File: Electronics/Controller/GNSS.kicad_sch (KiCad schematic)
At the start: 10 parts, among them J2 Conn_01x02, J3 Conn_01x02, J4 Conn_01x02, J5 Conn_01x02, J6 GPS SIM, J7 Conn_01x02, J8 Conn_01x02, U1 simpleRTK2B, U2 simpleRTK2B, U4 simpleRTK2B

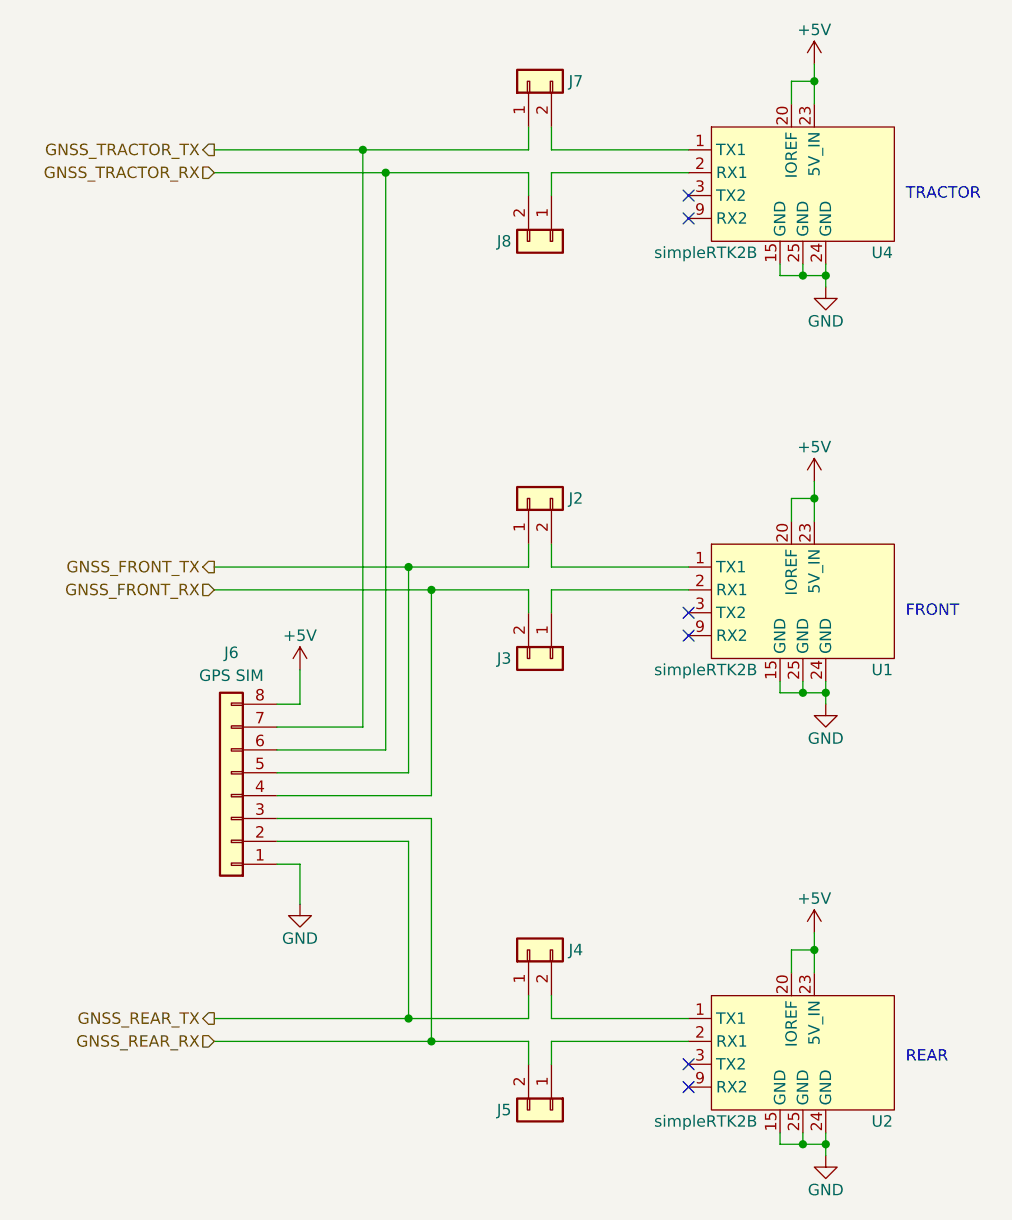
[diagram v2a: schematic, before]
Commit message: Updated schematic. Added footprints for all components.
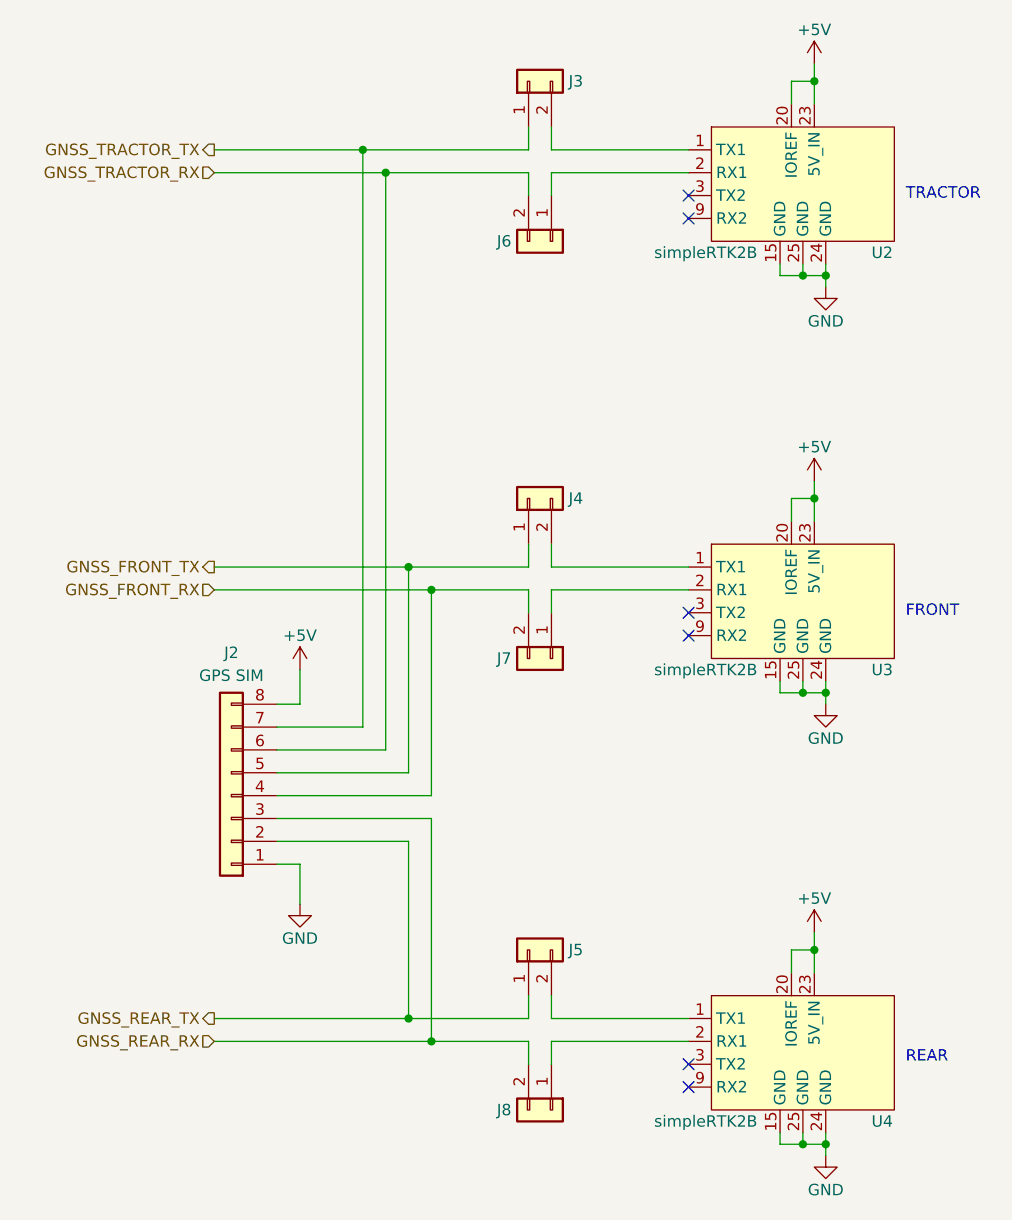
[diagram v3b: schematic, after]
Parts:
- J2: renamed from J6; footprint (none) -> Connector_PinHeader_2.54mm:PinHeader_2x04_P2.54mm_Vertical
- J3: renamed from J7; footprint (none) -> Connector_PinHeader_2.54mm:PinHeader_1x02_P2.54mm_Vertical
- J4: renamed from J2; footprint (none) -> Connector_PinHeader_2.54mm:PinHeader_1x02_P2.54mm_Vertical
- J5: renamed from J4; footprint (none) -> Connector_PinHeader_2.54mm:PinHeader_1x02_P2.54mm_Vertical
- J6: renamed from J8; footprint (none) -> Connector_PinHeader_2.54mm:PinHeader_1x02_P2.54mm_Vertical
- J7: renamed from J3; footprint (none) -> Connector_PinHeader_2.54mm:PinHeader_1x02_P2.54mm_Vertical
- J8: renamed from J5; footprint (none) -> Connector_PinHeader_2.54mm:PinHeader_1x02_P2.54mm_Vertical
- renumbered U4 to U2, U1 to U3, U2 to U4

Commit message: Moved controls from GPIO to CAN bus. Added two more CAN bus connectors. Changed GNSS SIM connector from pin header to JST-PH.
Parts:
- J2: footprint Connector_PinHeader_2.54mm:PinHeader_2x04_P2.54mm_Vertical -> Connector_JST:JST_PH_B8B-PH-K_1x08_P2.00mm_Vertical; manf# (none) -> B8B-PH-K-S
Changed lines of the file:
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@@
   (title_block
     (title "Tandem Leveller Controller")
-    (date "2025-02-19")
+    (date "2025-02-22")
     (rev "V1.0")
     (company "(C) andy@britishideas.com 2025")
@@
       (effects (font (size 1.27 1.27)))
     )
-    (property "Footprint" "Connector_PinHeader_2.54mm:PinHeader_2x04_P2.54mm_Vertical" (at 118.11 110.49 0)
+    (property "Footprint" "Connector_JST:JST_PH_B8B-PH-K_1x08_P2.00mm_Vertical" (at 118.11 110.49 0)
       (effects (font (size 1.27 1.27)) hide)
     )
@@
       (effects (font (size 1.27 1.27)) hide)
     )
+    (property "manf#" "B8B-PH-K-S" (at 118.11 110.49 0)
+      (effects (font (size 1.27 1.27)) hide)
+    )

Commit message: Added 4.7uF caps to FT232RL on controller.
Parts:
- J2: LCSC (none) -> C157974
- J3, J4, J5, J6, J7, J8: LCSC (none) -> C7494857
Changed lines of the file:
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@@
   (title_block
     (title "Tandem Leveller Controller")
-    (date "2025-02-22")
+    (date "2025-03-11")
     (rev "V1.0")
     (company "(C) andy@britishideas.com 2025")
@@
       (effects (font (size 1.27 1.27)) hide)
     )
+    (property "LCSC" "C7494857" (at 153.67 48.895 0)
+      (effects (font (size 1.27 1.27)) hide)
+    )
     (pin "2")
     (pin "1")
@@
     )
     (property "manf#" "B8B-PH-K-S" (at 118.11 110.49 0)
+      (effects (font (size 1.27 1.27)) hide)
+    )
+    (property "LCSC" "C157974" (at 118.11 110.49 0)
       (effects (font (size 1.27 1.27)) hide)
     )
@@
     )
     (property "Datasheet" "" (at 171.45 48.895 0)
+      (effects (font (size 1.27 1.27)) hide)
+    )
+    (property "LCSC" "" (at 171.45 48.895 0)
       (effects (font (size 1.27 1.27)) hide)
     )
@@
       (effects (font (size 1.27 1.27)) hide)
     )
+    (property "LCSC" "" (at 171.45 95.25 0)
+      (effects (font (size 1.27 1.27)) hide)
+    )
     (pin "21")
     (pin "26")
@@
       (effects (font (size 1.27 1.27)) hide)
     )
+    (property "LCSC" "C7494857" (at 151.13 77.47 0)
+      (effects (font (size 1.27 1.27)) hide)
+    )
     (pin "2")
     (pin "1")
@@
       (effects (font (size 1.27 1.27)) hide)
     )
+    (property "LCSC" "C7494857" (at 151.13 127.635 0)
+      (effects (font (size 1.27 1.27)) hide)
+    )
     (pin "2")
     (pin "1")
@@
       (effects (font (size 1.27 1.27)) hide)
     )
+    (property "LCSC" "C7494857" (at 151.13 31.115 0)
+      (effects (font (size 1.27 1.27)) hide)
+    )
     (pin "2")
     (pin "1")
@@
       (effects (font (size 1.27 1.27)) hide)
     )
+    (property "LCSC" "C7494857" (at 153.67 95.25 0)
+      (effects (font (size 1.27 1.27)) hide)
+    )
     (pin "2")
     (pin "1")
@@
     )
     (property "Datasheet" "" (at 171.45 145.415 0)
+      (effects (font (size 1.27 1.27)) hide)
+    )
+    (property "LCSC" "" (at 171.45 145.415 0)
       (effects (font (size 1.27 1.27)) hide)
     )
@@
       (effects (font (size 1.27 1.27)) hide)
     )
+    (property "LCSC" "C7494857" (at 153.67 145.415 0)
+      (effects (font (size 1.27 1.27)) hide)
+    )
